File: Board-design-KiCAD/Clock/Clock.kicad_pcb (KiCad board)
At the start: 2 copper layers, 51 parts, among them M1 SevSeg4Inch, M2 SevSeg4Inch, Y1 SevSeg1.8Inch, Y2 SevSeg1.8Inch, Y3 SevSeg1.8Inch, Y4 SevSeg1.8Inch

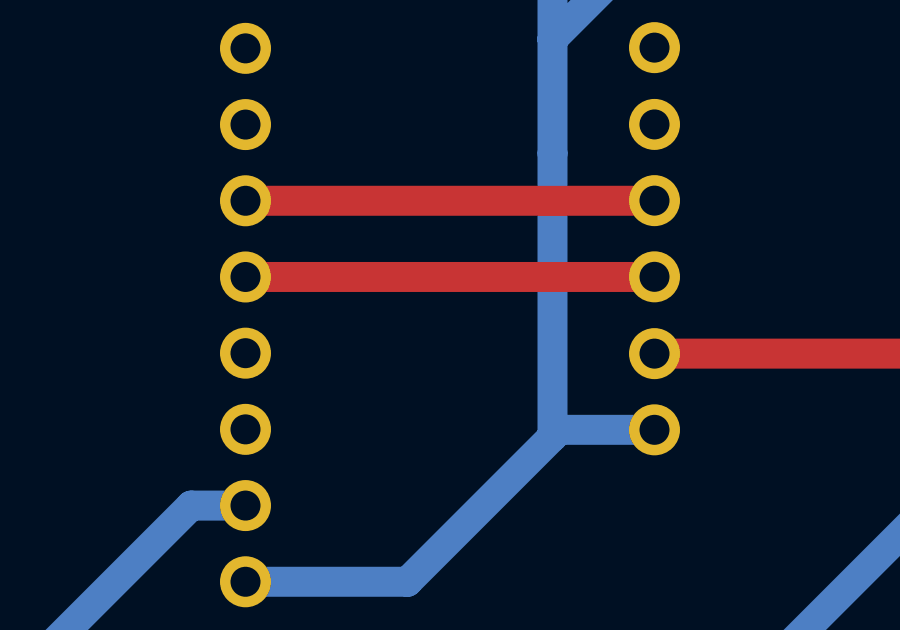
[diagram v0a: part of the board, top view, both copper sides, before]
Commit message: Use I2C on alternative pins. Code finished.
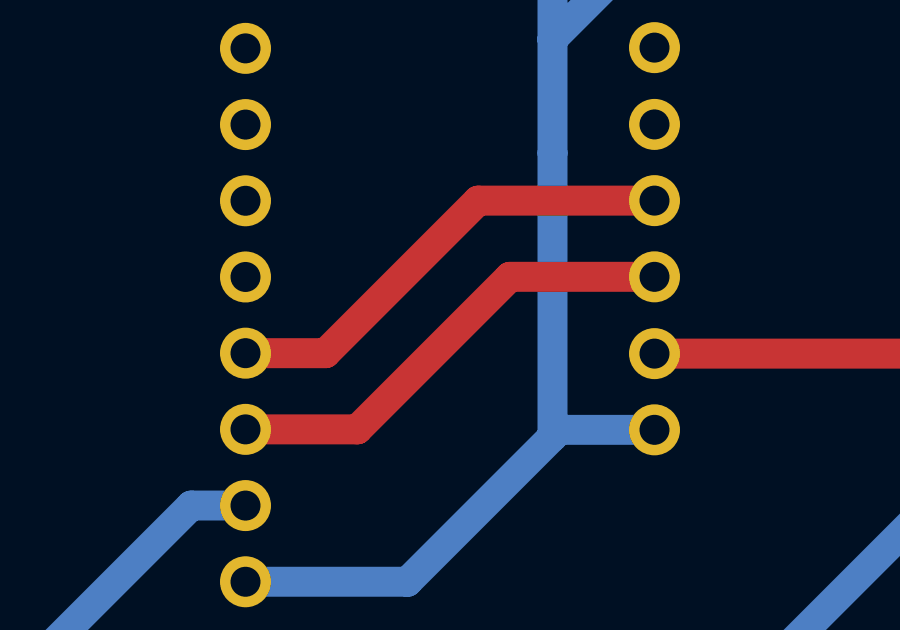
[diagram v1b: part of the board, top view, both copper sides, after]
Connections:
- MCU_1 pad 14: RTC_SCL -> Net-(MCU_1-Pad14)
- MCU_1 pad 15: RTC_SDA -> Net-(MCU_1-Pad15)
- MCU_1 pad 16: Net-(MCU_1-Pad16) -> RTC_SCL
- MCU_1 pad 17: Net-(MCU_1-Pad17) -> RTC_SDA
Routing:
- net RTC_SCL: track 13.6 -> 18.2 mm
- net RTC_SDA: track 13.6 -> 15.7 mm

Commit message: Add some names
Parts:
- 3.3V-Cin1, 3.3V-Cout1: value CP1 -> 10uF

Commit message: Fix some existing errors
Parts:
- added R_PULLUP_0: 1k, Resistor_THT:R_Axial_DIN0207_L6.3mm_D2.5mm_P10.16mm_Horizontal, B.Cu at (528.2, 69.4)
- added R_PULLUP_1: 1k, Resistor_THT:R_Axial_DIN0207_L6.3mm_D2.5mm_P10.16mm_Horizontal, B.Cu at (528.2, 62.6)
- added R_RST1: 1k, Resistor_THT:R_Axial_DIN0207_L6.3mm_D2.5mm_P10.16mm_Horizontal, B.Cu at (538.4, 66.0)
- BCD-DATE1, BCD-YEAR1: footprint Package_DIP:DIP-18_W7.62mm_LongPads -> Package_DIP:DIP-16_W7.62mm_Socket_LongPads
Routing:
- net +3.3V: track 112.8 -> 185.2 mm
- net (no net): track 0.00 -> 50.2 mm
- net Net-(MCU_2-Pad4): track 0.00 -> 50.1 mm
- net Net-(MCU_2-Pad6): track 0.00 -> 25.1 mm
- net Net-(MCU_2-Pad5): track 0.00 -> 18.7 mm
- net +6V: track 680.0 -> 693.1 mm
- net /YEAR_A: track 164.8 -> 155.7 mm
- net /DATE_E: track 255.0 -> 247.3 mm
- net /YEAR_G: track 204.6 -> 197.1 mm
- net /YEAR_F: track 181.8 -> 174.8 mm
- net /YEAR_D: track 207.4 -> 213.9 mm
- net /YEAR_B: track 226.2 -> 220.0 mm
- net GND: track 1511.3 -> 1505.7 mm
- net /DATE_C: track 234.2 -> 239.4 mm
- net +5V: track 790.9 -> 786.1 mm
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
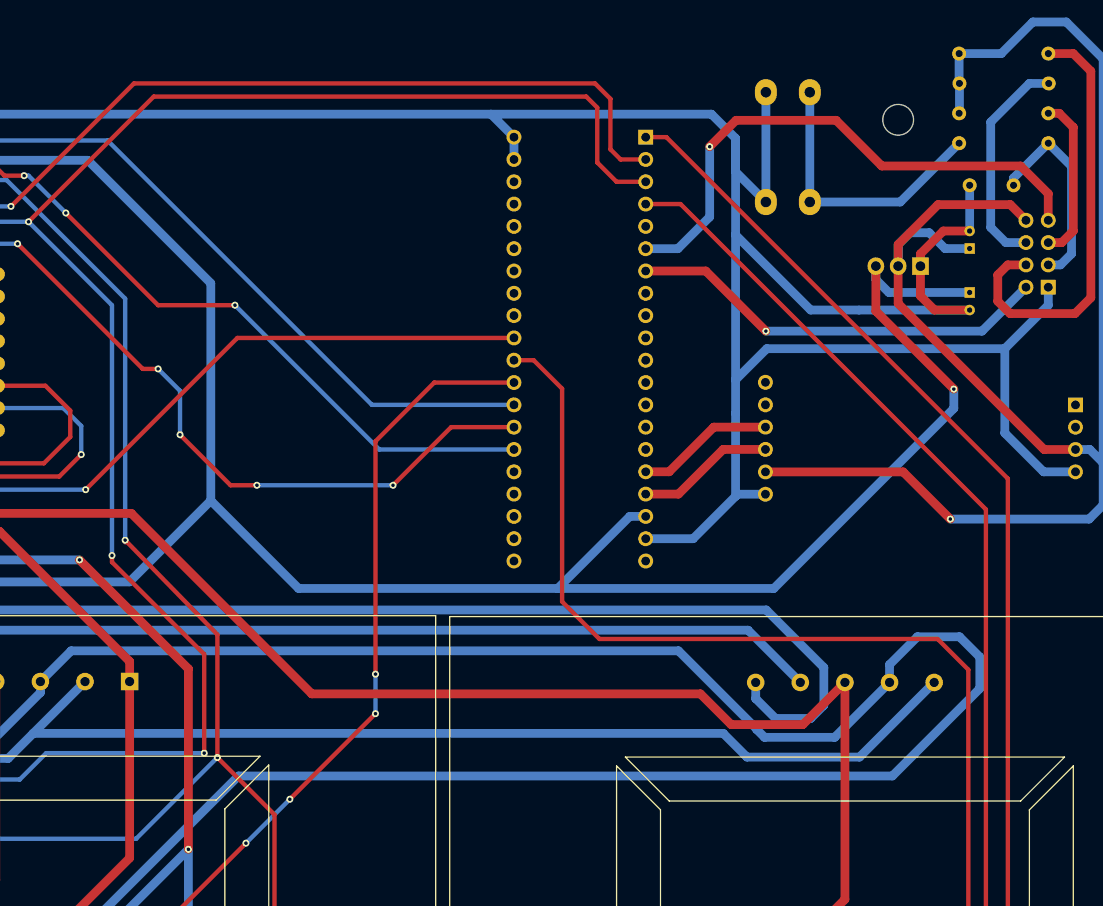
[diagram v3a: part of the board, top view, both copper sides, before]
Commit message: Rework on alarm function
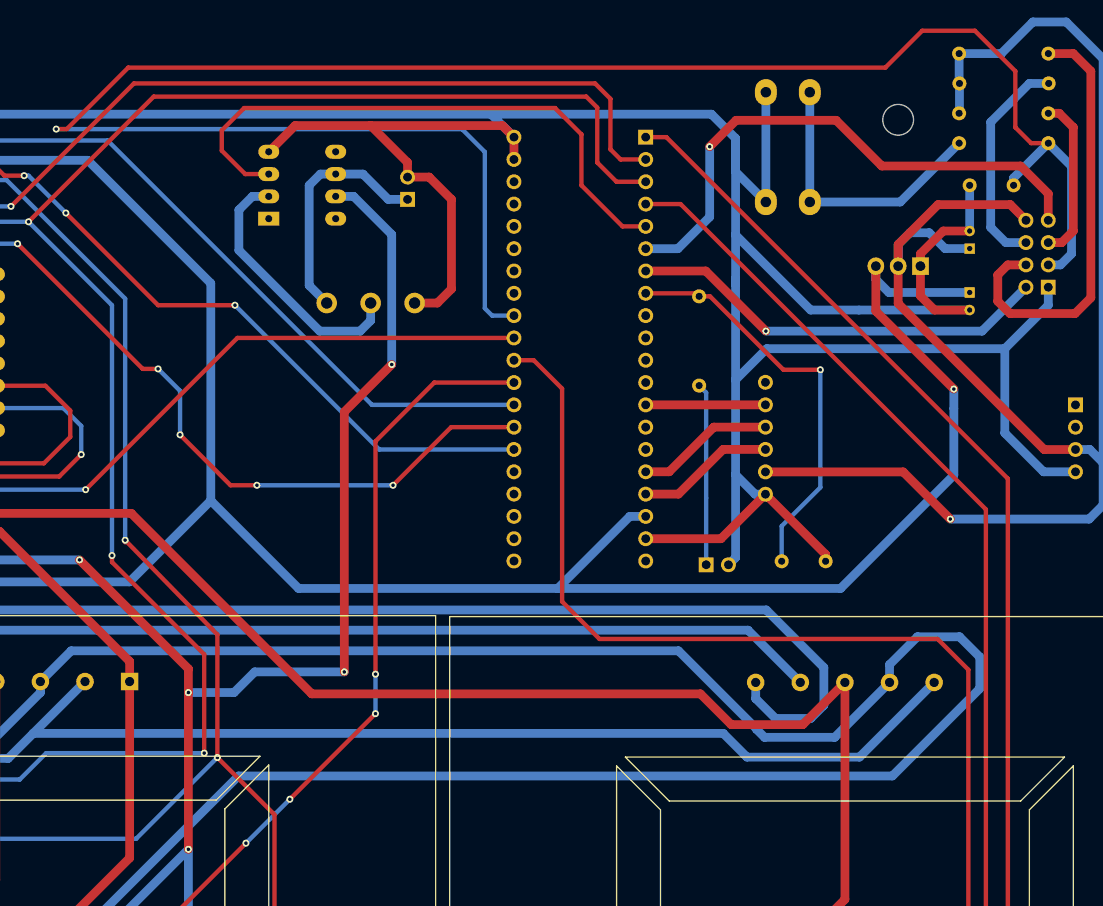
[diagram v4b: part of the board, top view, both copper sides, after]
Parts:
- added Debounce2: 10nF, Capacitor_THT:C_Disc_D5.0mm_W2.5mm_P5.00mm, B.Cu at (508.0, 120.4)
- added J1: Conn_01x02_Female, Connector_PinHeader_2.54mm:PinHeader_1x02_P2.54mm_Vertical, B.Cu at (465.4, 79.2)
- added J2: Conn_01x02_Female, Connector_PinHeader_2.54mm:PinHeader_1x02_P2.54mm_Vertical, B.Cu at (499.4, 120.8)
- added RV1: R_POT_US, Potentiometer_THT:Potentiometer_Piher_T-16H_Single_Horizontal, B.Cu at (466.2, 91.0)
- added R_BUTTON2: 350, Resistor_THT:R_Axial_DIN0207_L6.3mm_D2.5mm_P10.16mm_Horizontal, B.Cu at (498.6, 100.4)
- added U1: LM741, Package_DIP:DIP-8_W7.62mm_Socket_LongPads, B.Cu at (449.6, 81.4)
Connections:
- INVERTER_2 pad 12: (no net) -> Net-(INVERTER_2-Pad12)
- INVERTER_2 pad 13: (no net) -> Net-(INVERTER_2-Pad13)
- MCU_1 pad 13: Net-(MCU_1-Pad13) -> CLK_IN
- MCU_1 pad 32: Net-(MCU_1-Pad32) -> CredentialsReset
- MCU_1 pad 5: Net-(MCU_1-Pad5) -> ALARM_PWM
- MCU_1 pad 8: Net-(MCU_1-Pad8) -> VOLUME_TEST
- RTC1 pad 9: Net-(RTC1-Pad9) -> CLK_IN
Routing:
- net CredentialsReset: track 23.3 -> 221.3 mm, vias 0 -> 1
- net GND: track 1505.7 -> 1587.6 mm
- net +11V: track 603.4 -> 682.3 mm, vias 7 -> 10
- net ALARM_PWM: track 0.00 -> 67.1 mm
- net VOLUME_TEST: track 0.00 -> 47.1 mm, vias 0 -> 1
- net Net-(RV1-Pad2): track 0.00 -> 29.9 mm
- net Net-(J1-Pad1): track 0.00 -> 27.2 mm
- net Net-(J2-Pad1): track 0.00 -> 20.7 mm
- net CLK_IN: track 0.00 -> 13.6 mm
- net +5V: track 786.1 -> 790.5 mm

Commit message: Finish up PCB design and fix some minor firmware issue
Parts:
- added R_BUTTON_PULLUP1: 4.7k, Resistor_THT:R_Axial_DIN0207_L6.3mm_D2.5mm_P10.16mm_Horizontal, B.Cu at (535.8, 120.6)
- Debounce2: value 10nF -> 100nF; footprint Capacitor_THT:C_Disc_D5.0mm_W2.5mm_P5.00mm -> Custom:CP_Radial_H15.0mm_W14.0mm_T8.0mm_P8.5mm_Horizontal
- R_BUTTON2: value 350 -> 100
- moved R_BUTTON2 36.1 mm to (525.6, 124.4), turned to 0 degrees
- moved PowerSupply1 30.2 mm to (175.3, 278.1)
- moved Debounce2 7.15 mm to (514.8, 122.6)
- moved J2 2.61 mm to (502.0, 120.6), turned to 90 degrees
- moved Debounce1 1.01 mm to (533.4, 77.5)
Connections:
- Debounce2 pad 2: GND -> Net-(Debounce2-Pad2)
- J2 pad 1: Net-(J2-Pad1) -> VOLUME_TEST
- R_BUTTON2 pad 1: Net-(J2-Pad1) -> Net-(Debounce2-Pad2)
- R_BUTTON2 pad 2: VOLUME_TEST -> GND
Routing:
- net GND: track 1587.6 -> 1654.0 mm, vias 4 -> 7
- net /+15V: track 28.2 -> 58.7 mm
- net Net-(J2-Pad1): track 20.7 -> 0.00 mm
- net VOLUME_TEST: track 47.1 -> 63.9 mm, vias 1 -> 0
- net +3.3V: track 185.2 -> 194.5 mm
- net Net-(Debounce2-Pad2): track 0.00 -> 7.30 mm
- net +5V: track 790.5 -> 792.1 mm
- net Net-(MCU_2-Pad6): track 25.1 -> 25.9 mm
- net (no net): vias 0 -> 1
- added copper zone on B.Cu, net GND
- added copper zone on F.Cu, net GND
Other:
- board outline added: 419.1 x 292.1 mm

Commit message: Add mounting holes and generate gerber files
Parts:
- added REF**: MountingHole_3.2mm_M3_ISO7380, MountingHole:MountingHole_3.2mm_M3_ISO7380, F.Cu at (177.8, 52.1)
- added REF**: MountingHole_3.2mm_M3_ISO7380, MountingHole:MountingHole_3.2mm_M3_ISO7380, F.Cu at (571.5, 50.8)
- added REF**: MountingHole_3.2mm_M3_ISO7380, MountingHole:MountingHole_3.2mm_M3_ISO7380, F.Cu at (571.5, 317.5)
- added REF**: MountingHole_3.2mm_M3_ISO7380, MountingHole:MountingHole_3.2mm_M3_ISO7380, F.Cu at (177.8, 317.5)
- Debounce1: footprint Capacitor_THT:C_Disc_D5.0mm_W2.5mm_P5.00mm -> Custom:CP_Radial_H15.0mm_W14.0mm_T8.0mm_P8.5mm_Horizontal
- moved Debounce1 30.5 mm to (508.4, 60.0), turned to 0 degrees
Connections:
- Credentials_Reset1 pad 2: Net-(Credentials_Reset1-Pad2) -> CredentialsReset
- Debounce1 pad 2: GND -> Net-(Debounce1-Pad2)
- R_BUTTON1 pad 1: Net-(Credentials_Reset1-Pad2) -> GND
- R_BUTTON1 pad 2: CredentialsReset -> Net-(Debounce1-Pad2)
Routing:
- net Net-(Debounce1-Pad2): track 0.00 -> 34.7 mm
- net Net-(Credentials_Reset1-Pad2): track 32.3 -> 0.00 mm
- net GND: track 1654.0 -> 1658.7 mm, vias 7 -> 4
- net CredentialsReset: track 221.7 -> 220.9 mm, vias 1 -> 2
- net (no net): vias 1 -> 0

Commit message: Resolve problems raised from datasheets
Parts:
- removed the REF** at (177.8, 52.1)
- removed the REF** at (571.5, 50.8)
- removed the REF** at (571.5, 317.5)
- removed the REF** at (177.8, 317.5)
- added REF**: MountingHole_3.2mm_M3_ISO14580, MountingHole:MountingHole_3.2mm_M3_ISO14580, F.Cu at (177.8, 317.5)
- added REF**: MountingHole_3.2mm_M3_ISO14580, MountingHole:MountingHole_3.2mm_M3_ISO14580, F.Cu at (177.8, 50.8)
- added REF**: MountingHole_3.2mm_M3_ISO14580, MountingHole:MountingHole_3.2mm_M3_ISO14580, F.Cu at (571.5, 50.8)
- added REF**: MountingHole_3.2mm_M3_ISO14580, MountingHole:MountingHole_3.2mm_M3_ISO14580, F.Cu at (571.5, 317.5)
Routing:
- net (no net): track 50.2 -> 0.00 mm
- net GND: track 1658.7 -> 1692.8 mm
